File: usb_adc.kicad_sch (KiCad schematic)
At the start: 17 parts, among them IC1 PCM2903CDBR, U1 74LVC1G08, X1 ECS-120-8-36-CKM-TR3

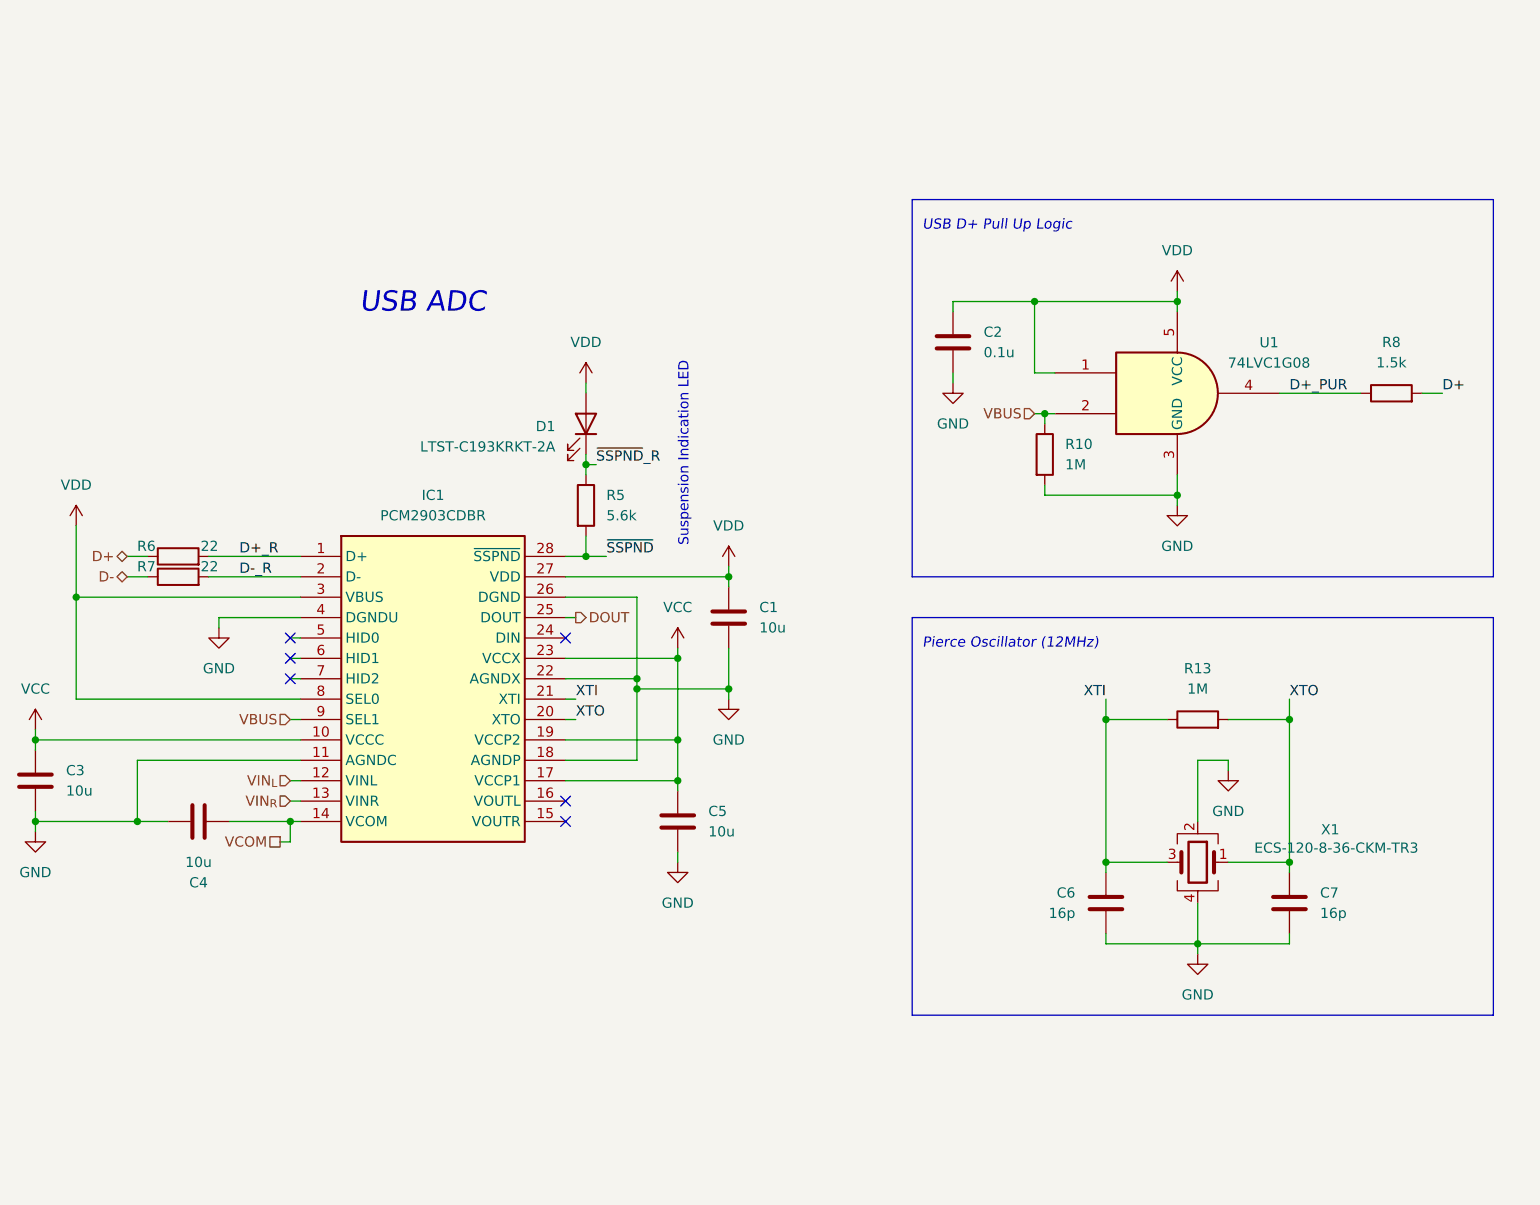
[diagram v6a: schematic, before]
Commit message: Starting layout
Also why are the mf diodes so small
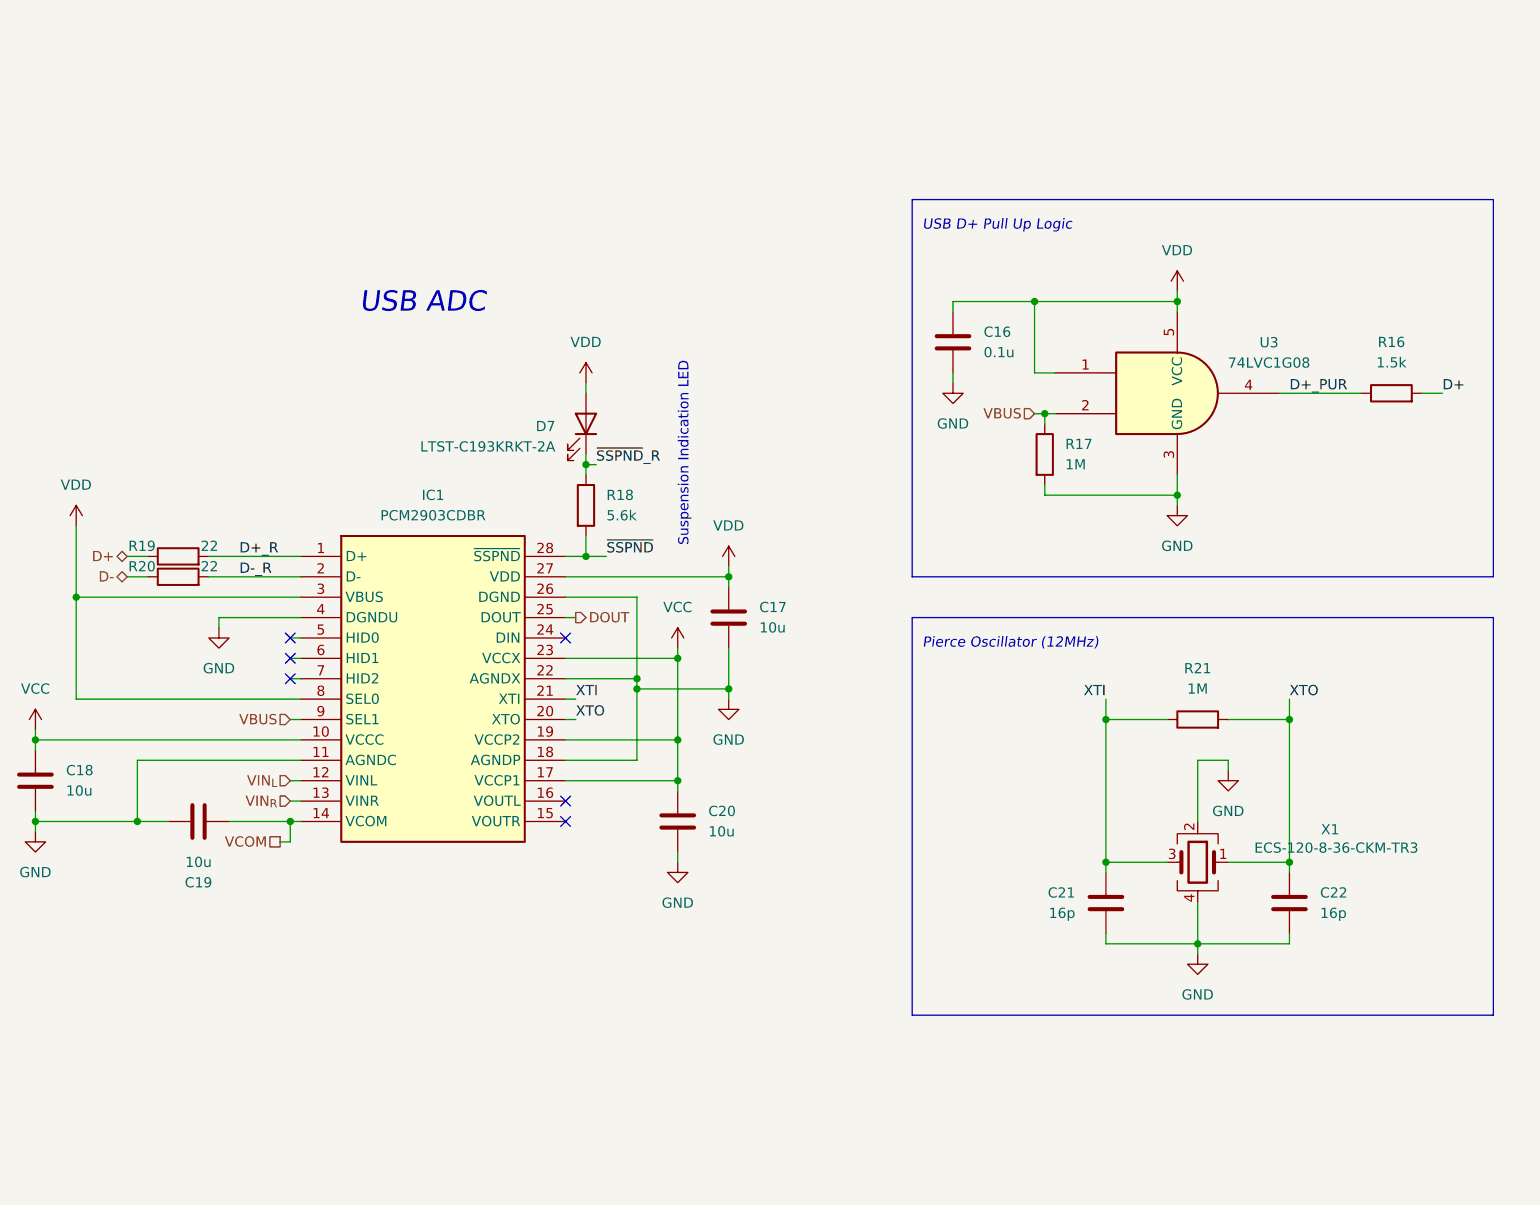
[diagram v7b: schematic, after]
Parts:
- renumbered C2 to C16, C1 to C17, C3 to C18, C4 to C19, C5 to C20, C6 to C21, C7 to C22, D1 to D7, R8 to R16, R10 to R17, R5 to R18, R6 to R19, R7 to R20, R13 to R21, U1 to U3
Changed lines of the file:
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@@
 		(dnp no)
 		(fields_autoplaced yes)
-		(property "Reference" "U1"
+		(property "Reference" "U3"
 			(at 217.17 55.9114 0)
 			(effects
@@
 			(project "BinauralMic"
 				(path "/d9e790b9-8aa4-4e58-8bd7-6ef4bc890627/1f1de066-50ca-4c06-9457-56cc25f04510"
-					(reference "U1")
+					(reference "U3")
 					(unit 1)
 				)
@@
 		(dnp no)
 		(fields_autoplaced yes)
-		(property "Reference" "C5"
+		(property "Reference" "C20"
 			(at 147.32 114.2999 0)
 			(effects
@@
 			(project "BinauralMic"
 				(path "/d9e790b9-8aa4-4e58-8bd7-6ef4bc890627/1f1de066-50ca-4c06-9457-56cc25f04510"
-					(reference "C5")
+					(reference "C20")
 					(unit 1)
 				)
@@
 		(dnp no)
 		(fields_autoplaced yes)
-		(property "Reference" "C1"
+		(property "Reference" "C17"
 			(at 153.67 88.8999 0)
 			(effects
@@
 			(project "BinauralMic"
 				(path "/d9e790b9-8aa4-4e58-8bd7-6ef4bc890627/1f1de066-50ca-4c06-9457-56cc25f04510"
-					(reference "C1")
+					(reference "C17")
 					(unit 1)
 				)
@@
 		(dnp no)
 		(fields_autoplaced yes)
-		(property "Reference" "C7"
+		(property "Reference" "C22"
 			(at 223.52 124.4599 0)
 			(effects
@@
 			(project "BinauralMic"
 				(path "/d9e790b9-8aa4-4e58-8bd7-6ef4bc890627/1f1de066-50ca-4c06-9457-56cc25f04510"
-					(reference "C7")
+					(reference "C22")
 					(unit 1)
 				)
@@
 		(dnp no)
 		(fields_autoplaced yes)
-		(property "Reference" "R13"
+		(property "Reference" "R21"
 			(at 208.28 96.52 90)
 			(effects
@@
 			(project "BinauralMic"
 				(path "/d9e790b9-8aa4-4e58-8bd7-6ef4bc890627/1f1de066-50ca-4c06-9457-56cc25f04510"
-					(reference "R13")
+					(reference "R21")
 					(unit 1)
 				)
@@
 		(dnp no)
 		(fields_autoplaced yes)
-		(property "Reference" "R8"
+		(property "Reference" "R16"
 			(at 232.41 55.88 90)
 			(effects
@@
 			(project "BinauralMic"
 				(path "/d9e790b9-8aa4-4e58-8bd7-6ef4bc890627/1f1de066-50ca-4c06-9457-56cc25f04510"
-					(reference "R8")
+					(reference "R16")
 					(unit 1)
 				)
@@
 		(dnp no)
 		(fields_autoplaced yes)
-		(property "Reference" "#PWR04"
+		(property "Reference" "#PWR023"
 			(at 149.86 87.63 0)
 			(effects
@@
 			(project "BinauralMic"
 				(path "/d9e790b9-8aa4-4e58-8bd7-6ef4bc890627/1f1de066-50ca-4c06-9457-56cc25f04510"
-					(reference "#PWR04")
+					(reference "#PWR023")
 					(unit 1)
 				)
@@
 		(dnp no)
 		(fields_autoplaced yes)
-		(property "Reference" "#PWR05"
+		(property "Reference" "#PWR024"
 			(at 86.36 97.79 0)
 			(effects
@@
 			(project "BinauralMic"
 				(path "/d9e790b9-8aa4-4e58-8bd7-6ef4bc890627/1f1de066-50ca-4c06-9457-56cc25f04510"
-					(reference "#PWR05")
+					(reference "#PWR024")
 					(unit 1)
 				)
@@
 		(dnp no)
 		(fields_autoplaced yes)
-		(property "Reference" "#PWR06"
+		(property "Reference" "#PWR025"
 			(at 143.51 97.79 0)
 			(effects
@@
 			(project "BinauralMic"
 				(path "/d9e790b9-8aa4-4e58-8bd7-6ef4bc890627/1f1de066-50ca-4c06-9457-56cc25f04510"
-					(reference "#PWR06")
+					(reference "#PWR025")
 					(unit 1)
 				)
@@
 		(dnp no)
 		(fields_autoplaced yes)
-		(property "Reference" "C2"
+		(property "Reference" "C16"
 			(at 181.61 54.6099 0)
 			(effects
@@
 			(project "BinauralMic"
 				(path "/d9e790b9-8aa4-4e58-8bd7-6ef4bc890627/1f1de066-50ca-4c06-9457-56cc25f04510"
-					(reference "C2")
+					(reference "C16")
 					(unit 1)
 				)
@@
 		(dnp no)
 		(fields_autoplaced yes)
-		(property "Reference" "#PWR08"
+		(property "Reference" "#PWR026"
 			(at 149.86 106.68 0)
 			(effects
@@
 			(project "BinauralMic"
 				(path "/d9e790b9-8aa4-4e58-8bd7-6ef4bc890627/1f1de066-50ca-4c06-9457-56cc25f04510"
-					(reference "#PWR08")
+					(reference "#PWR026")
 					(unit 1)
 				)
@@
 		(dnp no)
 		(fields_autoplaced yes)
-		(property "Reference" "R10"
+		(property "Reference" "R17"
 			(at 191.77 68.5799 0)
 			(effects
@@
 			(project "BinauralMic"
 				(path "/d9e790b9-8aa4-4e58-8bd7-6ef4bc890627/1f1de066-50ca-4c06-9457-56cc25f04510"
-					(reference "R10")
+					(reference "R17")
 					(unit 1)
 				)
@@
 		(dnp no)
 		(fields_autoplaced yes)
-		(property "Reference" "#PWR018"
+		(property "Reference" "#PWR028"
 			(at 212.09 115.57 0)
 			(effects
@@
 			(project "BinauralMic"
 				(path "/d9e790b9-8aa4-4e58-8bd7-6ef4bc890627/1f1de066-50ca-4c06-9457-56cc25f04510"
-					(reference "#PWR018")
+					(reference "#PWR028")
 					(unit 1)
 				)
@@
 		(dnp no)
 		(fields_autoplaced yes)
-		(property "Reference" "#PWR013"
+		(property "Reference" "#PWR021"
 			(at 205.74 82.55 0)
 			(effects
@@
 			(project "BinauralMic"
 				(path "/d9e790b9-8aa4-4e58-8bd7-6ef4bc890627/1f1de066-50ca-4c06-9457-56cc25f04510"
-					(reference "#PWR013")
+					(reference "#PWR021")
 					(unit 1)
 				)
@@
 		(dnp no)
 		(fields_autoplaced yes)
-		(property "Reference" "D1"
+		(property "Reference" "D7"
 			(at 128.27 66.3574 90)
 			(effects
@@
 			(project "BinauralMic"
 				(path "/d9e790b9-8aa4-4e58-8bd7-6ef4bc890627/1f1de066-50ca-4c06-9457-56cc25f04510"
-					(reference "D1")
+					(reference "D7")
 					(unit 1)
 				)
@@
 		(on_board yes)
 		(dnp no)
-		(property "Reference" "R6"
+		(property "Reference" "R19"
 			(at 78.486 81.28 90)
 			(effects
@@
 			(project "BinauralMic"
 				(path "/d9e790b9-8aa4-4e58-8bd7-6ef4bc890627/1f1de066-50ca-4c06-9457-56cc25f04510"
-					(reference "R6")
+					(reference "R19")
 					(unit 1)
 				)
@@
 		(dnp no)
 		(fields_autoplaced yes)
-		(property "Reference" "#PWR019"
+		(property "Reference" "#PWR031"
 			(at 208.28 138.43 0)
 			(effects
@@
 			(project "BinauralMic"
 				(path "/d9e790b9-8aa4-4e58-8bd7-6ef4bc890627/1f1de066-50ca-4c06-9457-56cc25f04510"
-					(reference "#PWR019")
+					(reference "#PWR031")
 					(unit 1)
 				)
@@
 		(dnp no)
 		(fields_autoplaced yes)
-		(property "Reference" "#PWR010"
+		(property "Reference" "#PWR020"
 			(at 177.8 67.31 0)
 			(effects
@@
 			(project "BinauralMic"
 				(path "/d9e790b9-8aa4-4e58-8bd7-6ef4bc890627/1f1de066-50ca-4c06-9457-56cc25f04510"
-					(reference "#PWR010")
+					(reference "#PWR020")
 					(unit 1)
 				)
@@
 		(dnp no)
 		(fields_autoplaced yes)
-		(property "Reference" "#PWR09"
+		(property "Reference" "#PWR027"
 			(at 63.5 107.95 0)
 			(effects
@@
 			(project "BinauralMic"
 				(path "/d9e790b9-8aa4-4e58-8bd7-6ef4bc890627/1f1de066-50ca-4c06-9457-56cc25f04510"
-					(reference "#PWR09")
+					(reference "#PWR027")
 					(unit 1)
 				)
@@
 		(on_board yes)
 		(dnp no)
-		(property "Reference" "C4"
+		(property "Reference" "C19"
 			(at 83.82 123.19 90)
 			(effects
@@
 			(project "BinauralMic"
 				(path "/d9e790b9-8aa4-4e58-8bd7-6ef4bc890627/1f1de066-50ca-4c06-9457-56cc25f04510"
-					(reference "C4")
+					(reference "C19")
 					(unit 1)
 				)
@@
 		(dnp no)
 		(fields_autoplaced yes)
-		(property "Reference" "#PWR02"
+		(property "Reference" "#PWR019"
 			(at 132.08 64.77 0)
 			(effects
@@
 			(project "BinauralMic"
 				(path "/d9e790b9-8aa4-4e58-8bd7-6ef4bc890627/1f1de066-50ca-4c06-9457-56cc25f04510"
-					(reference "#PWR02")
+					(reference "#PWR019")
 					(unit 1)
 				)
@@
 		(dnp no)
 		(fields_autoplaced yes)
-		(property "Reference" "C3"
+		(property "Reference" "C18"
 			(at 67.31 109.2199 0)
 			(effects
@@
 			(project "BinauralMic"
 				(path "/d9e790b9-8aa4-4e58-8bd7-6ef4bc890627/1f1de066-50ca-4c06-9457-56cc25f04510"
-					(reference "C3")
+					(reference "C18")
 					(unit 1)
 				)
@@
 		(on_board yes)
 		(dnp no)
-		(property "Reference" "R7"
+		(property "Reference" "R20"
 			(at 78.486 83.82 90)
 			(effects
@@
 			(project "BinauralMic"
 				(path "/d9e790b9-8aa4-4e58-8bd7-6ef4bc890627/1f1de066-50ca-4c06-9457-56cc25f04510"
-					(reference "R7")
+					(reference "R20")
 					(unit 1)
 				)
@@
 		(on_board yes)
 		(dnp no)
-		(property "Reference" "C6"
+		(property "Reference" "C21"
 			(at 193.04 124.4599 0)
 			(effects
@@
 			(project "BinauralMic"
 				(path "/d9e790b9-8aa4-4e58-8bd7-6ef4bc890627/1f1de066-50ca-4c06-9457-56cc25f04510"
-					(reference "C6")
+					(reference "C21")
 					(unit 1)
 				)
@@
 		(dnp no)
 		(fields_autoplaced yes)
-		(property "Reference" "#PWR011"
+		(property "Reference" "#PWR029"
 			(at 63.5 123.19 0)
 			(effects
@@
 			(project "BinauralMic"
 				(path "/d9e790b9-8aa4-4e58-8bd7-6ef4bc890627/1f1de066-50ca-4c06-9457-56cc25f04510"
-					(reference "#PWR011")
+					(reference "#PWR029")
 					(unit 1)
 				)
@@
 		(dnp no)
 		(fields_autoplaced yes)
-		(property "Reference" "R5"
+		(property "Reference" "R18"
 			(at 134.62 74.9299 0)
 			(effects
@@
 			(project "BinauralMic"
 				(path "/d9e790b9-8aa4-4e58-8bd7-6ef4bc890627/1f1de066-50ca-4c06-9457-56cc25f04510"
-					(reference "R5")
+					(reference "R18")
 					(unit 1)
 				)
@@
 		(dnp no)
 		(fields_autoplaced yes)
-		(property "Reference" "#PWR03"
+		(property "Reference" "#PWR022"
 			(at 68.58 82.55 0)
 			(effects
@@
 			(project "BinauralMic"
 				(path "/d9e790b9-8aa4-4e58-8bd7-6ef4bc890627/1f1de066-50ca-4c06-9457-56cc25f04510"
-					(reference "#PWR03")
+					(reference "#PWR022")
 					(unit 1)
 				)
@@
 		(dnp no)
 		(fields_autoplaced yes)
-		(property "Reference" "#PWR07"
+		(property "Reference" "#PWR018"
 			(at 205.74 53.34 0)
 			(effects
@@
 			(project "BinauralMic"
 				(path "/d9e790b9-8aa4-4e58-8bd7-6ef4bc890627/1f1de066-50ca-4c06-9457-56cc25f04510"
-					(reference "#PWR07")
+					(reference "#PWR018")
 					(unit 1)
 				)
@@
 		(dnp no)
 		(fields_autoplaced yes)
-		(property "Reference" "#PWR012"
+		(property "Reference" "#PWR030"
 			(at 143.51 127 0)
 			(effects
@@
 			(project "BinauralMic"
 				(path "/d9e790b9-8aa4-4e58-8bd7-6ef4bc890627/1f1de066-50ca-4c06-9457-56cc25f04510"
-					(reference "#PWR012")
-					(unit 1)
-				)
+					(reference "#PWR030")
+					(unit 1)
+				)
